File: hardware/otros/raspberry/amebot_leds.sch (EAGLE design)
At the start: 12 parts

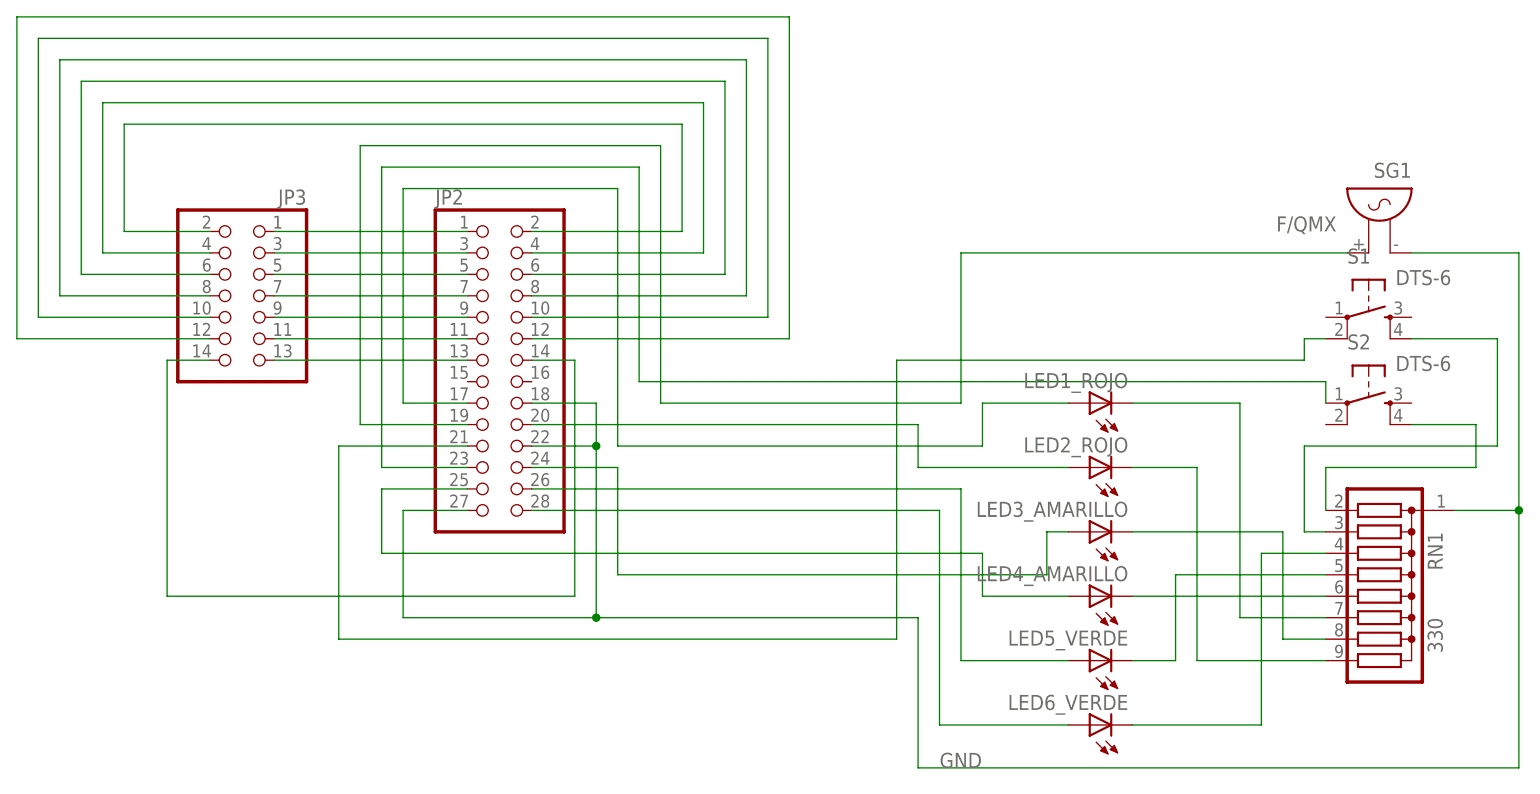
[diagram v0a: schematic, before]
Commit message: 
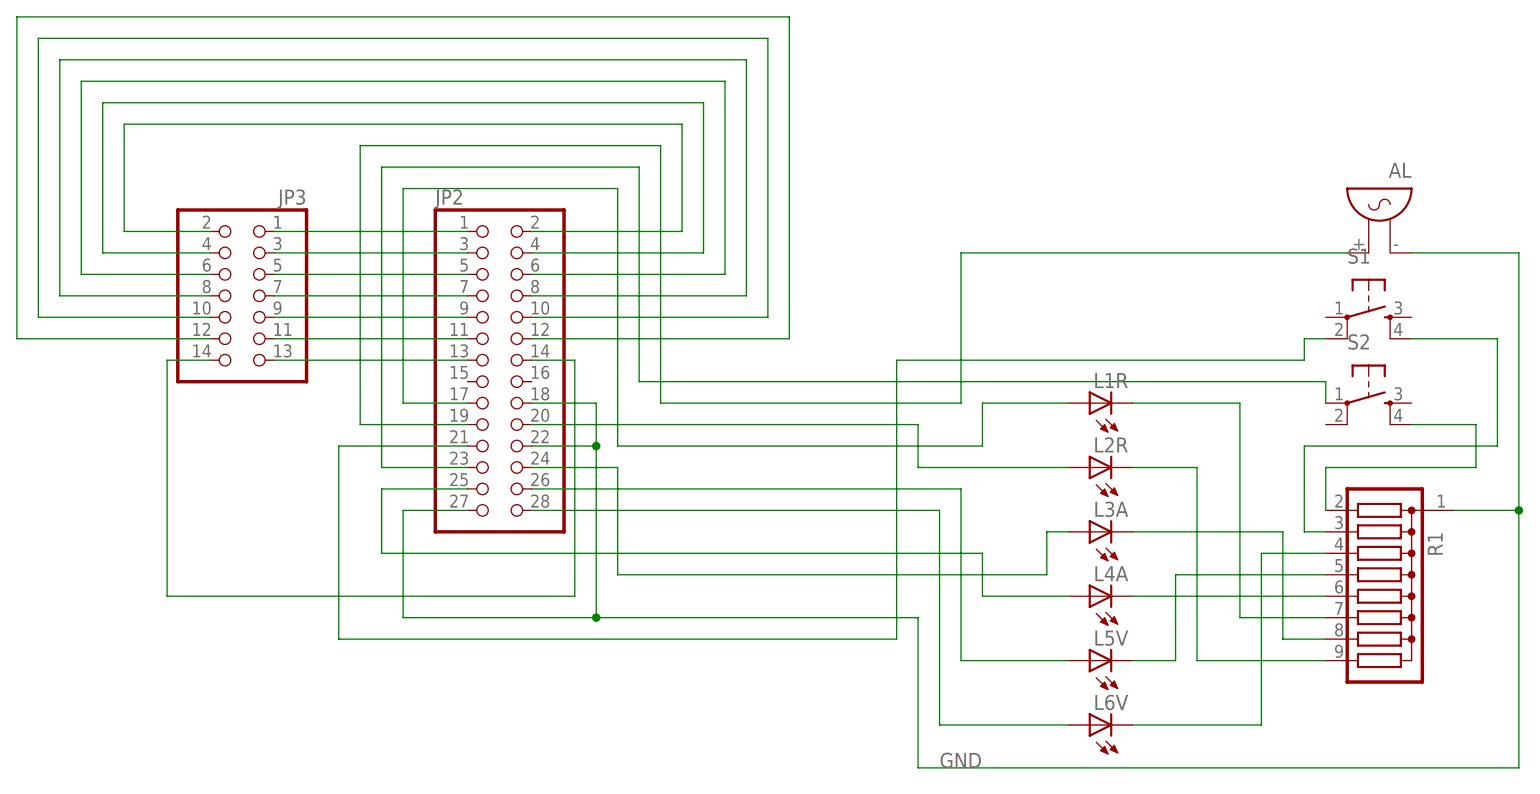
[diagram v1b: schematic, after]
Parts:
- R1: value 330 -> (none)
- renumbered LED1_ROJO to L1R, LED2_ROJO to L2R, LED3_AMARILLO to L3A, LED4_AMARILLO to L4A, LED5_VERDE to L5V, LED6_VERDE to L6V, RN1 to R1, SG1 to AL
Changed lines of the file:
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@@
 </classes>
 <parts>
-<part name="LED1_ROJO" library="led" deviceset="LED" device="5MM"/>
-<part name="LED2_ROJO" library="led" deviceset="LED" device="5MM"/>
-<part name="LED3_AMARILLO" library="led" deviceset="LED" device="5MM"/>
-<part name="LED4_AMARILLO" library="led" deviceset="LED" device="5MM"/>
-<part name="LED5_VERDE" library="led" deviceset="LED" device="5MM"/>
-<part name="LED6_VERDE" library="led" deviceset="LED" device="5MM"/>
-<part name="SG1" library="buzzer" deviceset="F/QMX" device=""/>
-<part name="S1" library="switch-tact" deviceset="DTS-6" device=""/>
-<part name="S2" library="switch-tact" deviceset="DTS-6" device=""/>
-<part name="RN1" library="resistor-sil" deviceset="G08R" device="" value="330"/>
+<part name="L1R" library="led" deviceset="LED" device="5MM"/>
+<part name="L2R" library="led" deviceset="LED" device="5MM"/>
+<part name="L3A" library="led" deviceset="LED" device="5MM"/>
+<part name="L4A" library="led" deviceset="LED" device="5MM"/>
+<part name="L5V" library="led" deviceset="LED" device="5MM"/>
+<part name="L6V" library="led" deviceset="LED" device="5MM"/>
+<part name="AL" library="buzzer" deviceset="F/QMX" device="" value=""/>
+<part name="S1" library="switch-tact" deviceset="DTS-6" device="" value=""/>
+<part name="S2" library="switch-tact" deviceset="DTS-6" device="" value=""/>
+<part name="R1" library="resistor-sil" deviceset="G08R" device=""/>
 <part name="JP2" library="pinhead" deviceset="PINHD-2X14" device=""/>
 <part name="JP3" library="pinhead" deviceset="PINHD-2X7" device=""/>
@@
 </plain>
 <instances>
-<instance part="LED1_ROJO" gate="G$1" x="22.86" y="68.58" rot="R90"/>
-<instance part="LED2_ROJO" gate="G$1" x="22.86" y="60.96" rot="R90"/>
-<instance part="LED3_AMARILLO" gate="G$1" x="22.86" y="53.34" rot="R90"/>
-<instance part="LED4_AMARILLO" gate="G$1" x="22.86" y="45.72" rot="R90"/>
-<instance part="LED5_VERDE" gate="G$1" x="22.86" y="38.1" rot="R90"/>
-<instance part="LED6_VERDE" gate="G$1" x="22.86" y="30.48" rot="R90"/>
-<instance part="SG1" gate="G$1" x="58.42" y="88.9" rot="MR0"/>
+<instance part="L1R" gate="G$1" x="22.86" y="68.58" rot="R90"/>
+<instance part="L2R" gate="G$1" x="22.86" y="60.96" rot="R90"/>
+<instance part="L3A" gate="G$1" x="22.86" y="53.34" rot="R90"/>
+<instance part="L4A" gate="G$1" x="22.86" y="45.72" rot="R90"/>
+<instance part="L5V" gate="G$1" x="22.86" y="38.1" rot="R90"/>
+<instance part="L6V" gate="G$1" x="22.86" y="30.48" rot="R90"/>
+<instance part="AL" gate="G$1" x="58.42" y="88.9" rot="MR0"/>
 <instance part="S1" gate="G$1" x="55.88" y="78.74" rot="R270"/>
 <instance part="S2" gate="G$1" x="55.88" y="68.58" rot="R270"/>
-<instance part="RN1" gate="G$1" x="55.88" y="45.72" rot="R270"/>
+<instance part="R1" gate="G$1" x="55.88" y="45.72" rot="R270"/>
 <instance part="JP2" gate="A" x="-48.26" y="73.66"/>
 <instance part="JP3" gate="A" x="-76.2" y="81.28" rot="MR0"/>
@@
 <segment>
 <wire x1="33.02" y1="48.26" x2="50.8" y2="48.26" width="0.1524" layer="91"/>
-<pinref part="RN1" gate="G$1" pin="5"/>
-<pinref part="LED5_VERDE" gate="G$1" pin="C"/>
+<pinref part="R1" gate="G$1" pin="5"/>
+<pinref part="L5V" gate="G$1" pin="C"/>
 <wire x1="27.94" y1="38.1" x2="33.02" y2="38.1" width="0.1524" layer="91"/>
 <wire x1="33.02" y1="48.26" x2="33.02" y2="38.1" width="0.1524" layer="91"/>
@@
 <net name="N$8" class="0">
 <segment>
-<pinref part="LED2_ROJO" gate="G$1" pin="C"/>
+<pinref part="L2R" gate="G$1" pin="C"/>
 <wire x1="27.94" y1="60.96" x2="35.56" y2="60.96" width="0.1524" layer="91"/>
 <wire x1="35.56" y1="60.96" x2="35.56" y2="38.1" width="0.1524" layer="91"/>
-<pinref part="RN1" gate="G$1" pin="9"/>
+<pinref part="R1" gate="G$1" pin="9"/>
 <wire x1="35.56" y1="38.1" x2="50.8" y2="38.1" width="0.1524" layer="91"/>
 </segment>
@@
 <net name="N$10" class="0">
 <segment>
-<pinref part="RN1" gate="G$1" pin="7"/>
+<pinref part="R1" gate="G$1" pin="7"/>
 <wire x1="40.64" y1="43.18" x2="50.8" y2="43.18" width="0.1524" layer="91"/>
-<pinref part="LED1_ROJO" gate="G$1" pin="C"/>
+<pinref part="L1R" gate="G$1" pin="C"/>
 <wire x1="27.94" y1="68.58" x2="40.64" y2="68.58" width="0.1524" layer="91"/>
 <wire x1="40.64" y1="68.58" x2="40.64" y2="43.18" width="0.1524" layer="91"/>
@@
 <net name="N$12" class="0">
 <segment>
-<pinref part="LED6_VERDE" gate="G$1" pin="C"/>
+<pinref part="L6V" gate="G$1" pin="C"/>
 <wire x1="27.94" y1="30.48" x2="43.18" y2="30.48" width="0.1524" layer="91"/>
 <wire x1="43.18" y1="30.48" x2="43.18" y2="50.8" width="0.1524" layer="91"/>
 <wire x1="43.18" y1="50.8" x2="50.8" y2="50.8" width="0.1524" layer="91"/>
-<pinref part="RN1" gate="G$1" pin="4"/>
+<pinref part="R1" gate="G$1" pin="4"/>
 </segment>
 </net>
 <net name="N$4" class="0">
 <segment>
-<pinref part="LED3_AMARILLO" gate="G$1" pin="C"/>
+<pinref part="L3A" gate="G$1" pin="C"/>
 <wire x1="27.94" y1="53.34" x2="45.72" y2="53.34" width="0.1524" layer="91"/>
 <wire x1="45.72" y1="53.34" x2="45.72" y2="40.64" width="0.1524" layer="91"/>
-<pinref part="RN1" gate="G$1" pin="8"/>
+<pinref part="R1" gate="G$1" pin="8"/>
 <wire x1="45.72" y1="40.64" x2="50.8" y2="40.64" width="0.1524" layer="91"/>
 </segment>
@@
 <net name="GND" class="0">
 <segment>
-<pinref part="SG1" gate="G$1" pin="1"/>
+<pinref part="AL" gate="G$1" pin="1"/>
 <wire x1="60.96" y1="86.36" x2="73.66" y2="86.36" width="0.1524" layer="91"/>
 <wire x1="73.66" y1="86.36" x2="73.66" y2="55.88" width="0.1524" layer="91"/>
@@
 <net name="N$15" class="0">
 <segment>
-<pinref part="RN1" gate="G$1" pin="2"/>
+<pinref part="R1" gate="G$1" pin="2"/>
 <wire x1="68.58" y1="60.96" x2="50.8" y2="60.96" width="0.1524" layer="91"/>
 <wire x1="50.8" y1="60.96" x2="50.8" y2="55.88" width="0.1524" layer="91"/>
@@
 <wire x1="71.12" y1="63.5" x2="48.26" y2="63.5" width="0.1524" layer="91"/>
 <wire x1="48.26" y1="63.5" x2="48.26" y2="53.34" width="0.1524" layer="91"/>
-<pinref part="RN1" gate="G$1" pin="3"/>
+<pinref part="R1" gate="G$1" pin="3"/>
 <wire x1="48.26" y1="53.34" x2="50.8" y2="53.34" width="0.1524" layer="91"/>
 </segment>
@@
 <net name="N$7" class="0">
 <segment>
-<pinref part="LED4_AMARILLO" gate="G$1" pin="C"/>
-<pinref part="RN1" gate="G$1" pin="6"/>
+<pinref part="L4A" gate="G$1" pin="C"/>
+<pinref part="R1" gate="G$1" pin="6"/>
 <wire x1="27.94" y1="45.72" x2="50.8" y2="45.72" width="0.1524" layer="91"/>
 </segment>
@@
 <wire x1="-27.94" y1="99.06" x2="-27.94" y2="68.58" width="0.1524" layer="91"/>
 <wire x1="7.62" y1="68.58" x2="7.62" y2="86.36" width="0.1524" layer="91"/>
-<pinref part="SG1" gate="G$1" pin="2"/>
+<pinref part="AL" gate="G$1" pin="2"/>
 <wire x1="7.62" y1="86.36" x2="53.34" y2="86.36" width="0.1524" layer="91"/>
 <pinref part="JP2" gate="A" pin="19"/>
@@
 <wire x1="-33.02" y1="48.26" x2="17.78" y2="48.26" width="0.1524" layer="91"/>
 <wire x1="17.78" y1="48.26" x2="17.78" y2="53.34" width="0.1524" layer="91"/>
-<pinref part="LED3_AMARILLO" gate="G$1" pin="A"/>
+<pinref part="L3A" gate="G$1" pin="A"/>
 <wire x1="17.78" y1="53.34" x2="20.32" y2="53.34" width="0.1524" layer="91"/>
 <pinref part="JP2" gate="A" pin="24"/>
@@
 <segment>
 <pinref part="JP2" gate="A" pin="28"/>
-<pinref part="LED6_VERDE" gate="G$1" pin="A"/>
+<pinref part="L6V" gate="G$1" pin="A"/>
 <wire x1="5.08" y1="30.48" x2="20.32" y2="30.48" width="0.1524" layer="91"/>
 <wire x1="-43.18" y1="55.88" x2="5.08" y2="55.88" width="0.1524" layer="91"/>
@@
 <pinref part="JP2" gate="A" pin="26"/>
 <wire x1="7.62" y1="58.42" x2="7.62" y2="38.1" width="0.1524" layer="91"/>
-<pinref part="LED5_VERDE" gate="G$1" pin="A"/>
+<pinref part="L5V" gate="G$1" pin="A"/>
 <wire x1="7.62" y1="38.1" x2="20.32" y2="38.1" width="0.1524" layer="91"/>
 </segment>
@@
 <wire x1="-50.8" y1="58.42" x2="-60.96" y2="58.42" width="0.1524" layer="91"/>
 <wire x1="-60.96" y1="58.42" x2="-60.96" y2="50.8" width="0.1524" layer="91"/>
-<pinref part="LED4_AMARILLO" gate="G$1" pin="A"/>
+<pinref part="L4A" gate="G$1" pin="A"/>
 <wire x1="10.16" y1="45.72" x2="20.32" y2="45.72" width="0.1524" layer="91"/>
 <wire x1="-60.96" y1="50.8" x2="10.16" y2="50.8" width="0.1524" layer="91"/>
@@
 <wire x1="-33.02" y1="63.5" x2="10.16" y2="63.5" width="0.1524" layer="91"/>
 <wire x1="10.16" y1="63.5" x2="10.16" y2="68.58" width="0.1524" layer="91"/>
-<pinref part="LED1_ROJO" gate="G$1" pin="A"/>
+<pinref part="L1R" gate="G$1" pin="A"/>
 <wire x1="10.16" y1="68.58" x2="20.32" y2="68.58" width="0.1524" layer="91"/>
 <wire x1="-33.02" y1="93.98" x2="-33.02" y2="63.5" width="0.1524" layer="91"/>
@@
 <net name="N$9" class="0">
 <segment>
-<pinref part="LED2_ROJO" gate="G$1" pin="A"/>
+<pinref part="L2R" gate="G$1" pin="A"/>
 <wire x1="20.32" y1="60.96" x2="2.54" y2="60.96" width="0.1524" layer="91"/>
 <wire x1="2.54" y1="60.96" x2="2.54" y2="66.04" width="0.1524" layer="91"/>

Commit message: 
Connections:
- removed net N$11: AL.2, JP2.19
- new net N$3: AL.2, JP2.25
- net N$13: now also JP2.17, S1.1; no longer JP2.21, S1.2
- net N$2: now also JP2.23; no longer JP2.17
- net N$21: now also L2R.A; no longer L3A.A
- net N$5: now also JP2.15; no longer JP2.23
- net N$6: now also JP2.19; no longer JP2.25
- net N$9: now also L3A.A; no longer L2R.A
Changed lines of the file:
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@@
 <net name="N$5" class="0">
 <segment>
-<wire x1="-60.96" y1="60.96" x2="-60.96" y2="96.52" width="0.1524" layer="91"/>
+<wire x1="-60.96" y1="71.12" x2="-60.96" y2="96.52" width="0.1524" layer="91"/>
 <wire x1="-60.96" y1="96.52" x2="-30.48" y2="96.52" width="0.1524" layer="91"/>
 <wire x1="-30.48" y1="96.52" x2="-30.48" y2="71.12" width="0.1524" layer="91"/>
@@
 <wire x1="50.8" y1="71.12" x2="50.8" y2="68.58" width="0.1524" layer="91"/>
 <wire x1="-30.48" y1="71.12" x2="50.8" y2="71.12" width="0.1524" layer="91"/>
-<pinref part="JP2" gate="A" pin="23"/>
-<wire x1="-60.96" y1="60.96" x2="-50.8" y2="60.96" width="0.1524" layer="91"/>
-</segment>
-</net>
-<net name="N$11" class="0">
-<segment>
-<wire x1="-63.5" y1="66.04" x2="-63.5" y2="99.06" width="0.1524" layer="91"/>
-<wire x1="-63.5" y1="99.06" x2="-27.94" y2="99.06" width="0.1524" layer="91"/>
-<wire x1="-27.94" y1="68.58" x2="7.62" y2="68.58" width="0.1524" layer="91"/>
-<wire x1="-27.94" y1="99.06" x2="-27.94" y2="68.58" width="0.1524" layer="91"/>
-<wire x1="7.62" y1="68.58" x2="7.62" y2="86.36" width="0.1524" layer="91"/>
-<pinref part="AL" gate="G$1" pin="2"/>
-<wire x1="7.62" y1="86.36" x2="53.34" y2="86.36" width="0.1524" layer="91"/>
-<pinref part="JP2" gate="A" pin="19"/>
-<wire x1="-63.5" y1="66.04" x2="-50.8" y2="66.04" width="0.1524" layer="91"/>
+<pinref part="JP2" gate="A" pin="15"/>
+<wire x1="-60.96" y1="71.12" x2="-50.8" y2="71.12" width="0.1524" layer="91"/>
 </segment>
 </net>
 <net name="N$21" class="0">
 <segment>
-<wire x1="-33.02" y1="48.26" x2="17.78" y2="48.26" width="0.1524" layer="91"/>
-<wire x1="17.78" y1="48.26" x2="17.78" y2="53.34" width="0.1524" layer="91"/>
-<pinref part="L3A" gate="G$1" pin="A"/>
-<wire x1="17.78" y1="53.34" x2="20.32" y2="53.34" width="0.1524" layer="91"/>
+<wire x1="-33.02" y1="48.26" x2="12.7" y2="48.26" width="0.1524" layer="91"/>
 <pinref part="JP2" gate="A" pin="24"/>
 <wire x1="-43.18" y1="60.96" x2="-33.02" y2="60.96" width="0.1524" layer="91"/>
 <wire x1="-33.02" y1="60.96" x2="-33.02" y2="48.26" width="0.1524" layer="91"/>
+<pinref part="L2R" gate="G$1" pin="A"/>
+<wire x1="20.32" y1="60.96" x2="12.7" y2="60.96" width="0.1524" layer="91"/>
+<wire x1="12.7" y1="48.26" x2="12.7" y2="60.96" width="0.1524" layer="91"/>
 </segment>
 </net>
@@
 <net name="N$6" class="0">
 <segment>
-<pinref part="JP2" gate="A" pin="25"/>
-<wire x1="-50.8" y1="58.42" x2="-60.96" y2="58.42" width="0.1524" layer="91"/>
-<wire x1="-60.96" y1="58.42" x2="-60.96" y2="50.8" width="0.1524" layer="91"/>
 <pinref part="L4A" gate="G$1" pin="A"/>
 <wire x1="10.16" y1="45.72" x2="20.32" y2="45.72" width="0.1524" layer="91"/>
 <wire x1="-60.96" y1="50.8" x2="10.16" y2="50.8" width="0.1524" layer="91"/>
 <wire x1="10.16" y1="50.8" x2="10.16" y2="45.72" width="0.1524" layer="91"/>
+<pinref part="JP2" gate="A" pin="19"/>
+<wire x1="-60.96" y1="66.04" x2="-50.8" y2="66.04" width="0.1524" layer="91"/>
+<wire x1="-60.96" y1="50.8" x2="-60.96" y2="66.04" width="0.1524" layer="91"/>
 </segment>
 </net>
@@
 <segment>
 <wire x1="-58.42" y1="93.98" x2="-33.02" y2="93.98" width="0.1524" layer="91"/>
-<pinref part="JP2" gate="A" pin="17"/>
-<wire x1="-50.8" y1="68.58" x2="-58.42" y2="68.58" width="0.1524" layer="91"/>
-<wire x1="-58.42" y1="68.58" x2="-58.42" y2="93.98" width="0.1524" layer="91"/>
+<wire x1="-58.42" y1="60.96" x2="-58.42" y2="93.98" width="0.1524" layer="91"/>
 <wire x1="-33.02" y1="63.5" x2="10.16" y2="63.5" width="0.1524" layer="91"/>
 <wire x1="10.16" y1="63.5" x2="10.16" y2="68.58" width="0.1524" layer="91"/>
@@
 <wire x1="10.16" y1="68.58" x2="20.32" y2="68.58" width="0.1524" layer="91"/>
 <wire x1="-33.02" y1="93.98" x2="-33.02" y2="63.5" width="0.1524" layer="91"/>
+<pinref part="JP2" gate="A" pin="23"/>
+<wire x1="-58.42" y1="60.96" x2="-50.8" y2="60.96" width="0.1524" layer="91"/>
 </segment>
 </net>
 <net name="N$9" class="0">
 <segment>
-<pinref part="L2R" gate="G$1" pin="A"/>
-<wire x1="20.32" y1="60.96" x2="2.54" y2="60.96" width="0.1524" layer="91"/>
-<wire x1="2.54" y1="60.96" x2="2.54" y2="66.04" width="0.1524" layer="91"/>
 <pinref part="JP2" gate="A" pin="20"/>
-<wire x1="2.54" y1="66.04" x2="-43.18" y2="66.04" width="0.1524" layer="91"/>
+<wire x1="17.78" y1="66.04" x2="-43.18" y2="66.04" width="0.1524" layer="91"/>
+<pinref part="L3A" gate="G$1" pin="A"/>
+<wire x1="17.78" y1="53.34" x2="20.32" y2="53.34" width="0.1524" layer="91"/>
+<wire x1="17.78" y1="66.04" x2="17.78" y2="53.34" width="0.1524" layer="91"/>
 </segment>
 </net>
 <net name="N$13" class="0">
 <segment>
-<wire x1="-66.04" y1="63.5" x2="-66.04" y2="40.64" width="0.1524" layer="91"/>
+<wire x1="-66.04" y1="68.58" x2="-66.04" y2="40.64" width="0.1524" layer="91"/>
 <wire x1="0" y1="73.66" x2="48.26" y2="73.66" width="0.1524" layer="91"/>
 <wire x1="-66.04" y1="40.64" x2="0" y2="40.64" width="0.1524" layer="91"/>
 <wire x1="0" y1="40.64" x2="0" y2="73.66" width="0.1524" layer="91"/>
-<pinref part="JP2" gate="A" pin="21"/>
-<wire x1="-66.04" y1="63.5" x2="-50.8" y2="63.5" width="0.1524" layer="91"/>
-<pinref part="S1" gate="G$1" pin="2"/>
-<wire x1="50.8" y1="76.2" x2="48.26" y2="76.2" width="0.1524" layer="91"/>
-<wire x1="48.26" y1="76.2" x2="48.26" y2="73.66" width="0.1524" layer="91"/>
-</segment>
-</net>
+<wire x1="48.26" y1="73.66" x2="48.26" y2="78.74" width="0.1524" layer="91"/>
+<pinref part="S1" gate="G$1" pin="1"/>
+<wire x1="48.26" y1="78.74" x2="50.8" y2="78.74" width="0.1524" layer="91"/>
+<pinref part="JP2" gate="A" pin="17"/>
+<wire x1="-66.04" y1="68.58" x2="-50.8" y2="68.58" width="0.1524" layer="91"/>
+</segment>
+</net>
+<net name="N$3" class="0">
+<segment>
+<pinref part="JP2" gate="A" pin="25"/>
+<wire x1="-50.8" y1="58.42" x2="-63.5" y2="58.42" width="0.1524" layer="91"/>
+<wire x1="-63.5" y1="99.06" x2="-27.94" y2="99.06" width="0.1524" layer="91"/>
+<wire x1="-27.94" y1="68.58" x2="7.62" y2="68.58" width="0.1524" layer="91"/>
+<wire x1="-27.94" y1="99.06" x2="-27.94" y2="68.58" width="0.1524" layer="91"/>
+<wire x1="7.62" y1="68.58" x2="7.62" y2="86.36" width="0.1524" layer="91"/>
+<pinref part="AL" gate="G$1" pin="2"/>
+<wire x1="7.62" y1="86.36" x2="53.34" y2="86.36" width="0.1524" layer="91"/>
+<wire x1="-63.5" y1="58.42" x2="-63.5" y2="99.06" width="0.1524" layer="91"/>
+</segment>
+</net>
